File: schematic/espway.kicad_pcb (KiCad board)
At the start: 2 copper layers, 28 parts, among them J1 CONN_01X02, J2 CONN_01X02, J3 CONN_01X04_MALE, SW1 SW_Push, U1 DRV8835, U2 LM1117-3.3, U3 ESP-12E, U4 LSM6DS3

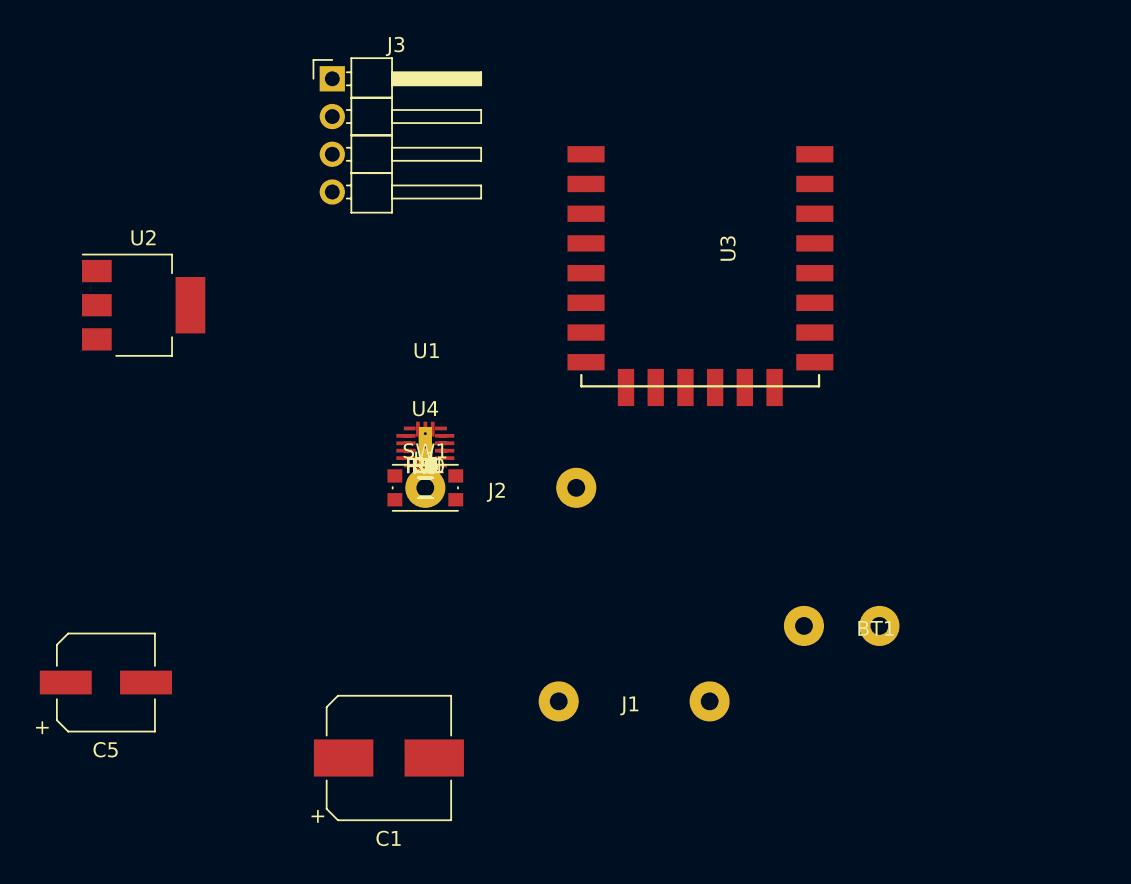
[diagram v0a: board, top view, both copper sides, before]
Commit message: Update schematic and PCB layout
Misses power led and routing
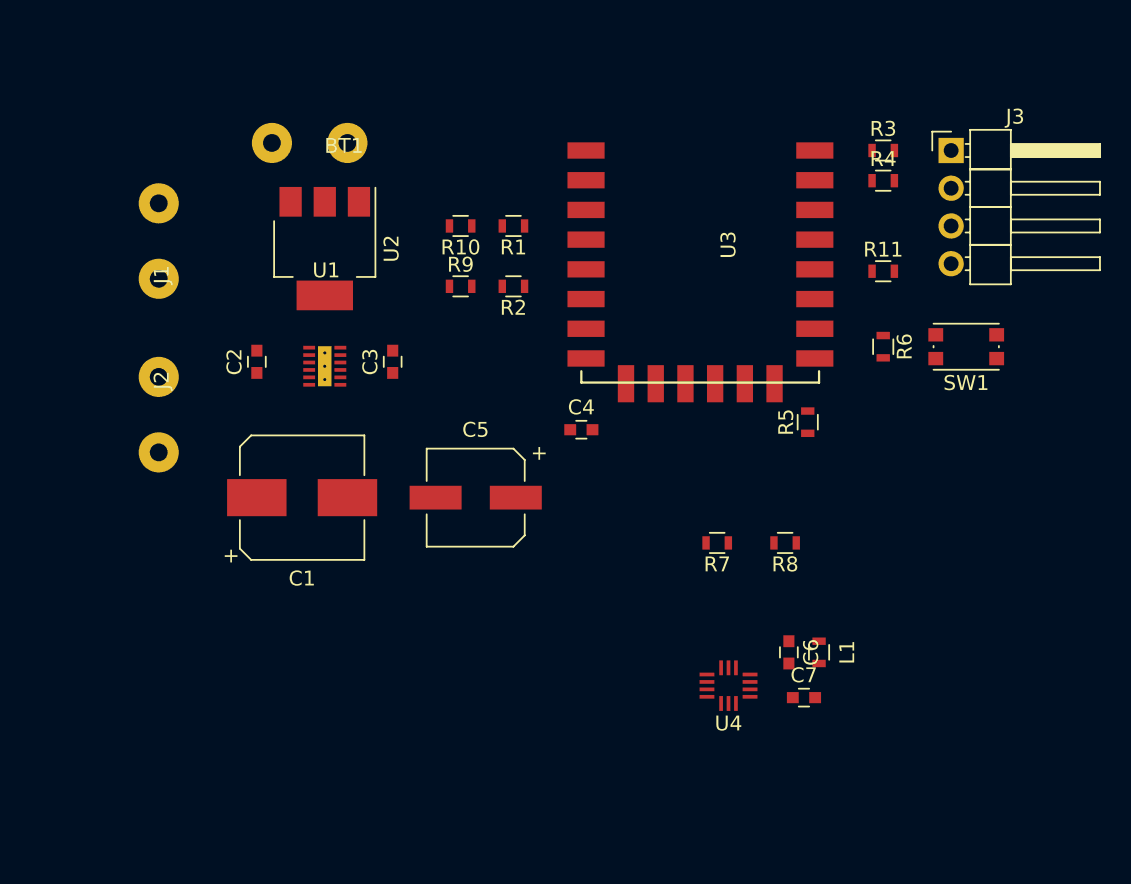
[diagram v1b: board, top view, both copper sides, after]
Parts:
- moved BT1 48.4 mm to (138.2, 81.8)
- moved J3 41.9 mm to (183.9, 82.3)
- moved R3 38.3 mm to (179.3, 82.3)
- moved SW1 37.6 mm to (184.9, 95.5), turned to 180 degrees
- moved R4 37.1 mm to (179.3, 84.3)
- moved J1 36.0 mm to (130.6, 95.5), turned to 90 degrees
- moved R11 34.1 mm to (179.3, 90.4)
- moved R6 32.3 mm to (179.3, 95.5), turned to 270 degrees
- moved C7 29.1 mm to (174.0, 119.1)
- moved L1 28.7 mm to (175.0, 116.1), turned to 270 degrees
- moved C5 27.8 mm to (151.9, 105.7), turned to 180 degrees
- moved C6 26.9 mm to (173.0, 116.1), turned to 270 degrees
- moved R5 26.1 mm to (174.2, 100.6), turned to 90 degrees
- moved R8 24.5 mm to (172.7, 108.7), turned to 180 degrees
- moved U4 23.0 mm to (168.9, 115.6), turned to 180 degrees
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
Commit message: Schematic and PCB update
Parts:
- U3: value ESP-12E -> ESP-12S
- moved C7 15.4 mm to (165.6, 106.2), turned to 270 degrees
- moved L1 9.01 mm to (169.2, 109.2), turned to 180 degrees
- moved R8 8.23 mm to (171.4, 100.6), turned to 90 degrees
- moved R7 8.14 mm to (168.7, 100.6), turned to 90 degrees
- moved U4 7.69 mm to (169.9, 108.0), turned to 0 degrees
- moved C6 6.86 mm to (173.0, 109.2), turned to 180 degrees
- moved J2 4.07 mm to (130.8, 106.7)
- moved J1 3.57 mm to (130.8, 99.1)
- moved R6 1.27 mm to (179.3, 94.2), turned to 0 degrees
- moved C4 0.51 mm to (159.0, 100.6), turned to 270 degrees

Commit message: Update schematic and PCB
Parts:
- added D1: LED, LEDs:LED_0603, F.Cu at (156.0, 98.0)
- added R12: 470, Resistors_SMD:R_0603, F.Cu at (156.2, 96.3)
- added REF**: MountingHole_2.2mm_M2, Mounting_Holes:MountingHole_2.2mm_M2, F.Cu at (177.0, 115.6)
- added REF**: MountingHole_2.2mm_M2, Mounting_Holes:MountingHole_2.2mm_M2, F.Cu at (147.3, 115.6)
- added REF**: MountingHole_2.2mm_M2, Mounting_Holes:MountingHole_2.2mm_M2, F.Cu at (147.3, 83.1)
- J1, J2: footprint Wire_Connections_Bridges:WireConnection_1.20mmDrill -> Wire_Connections_Bridges:WireConnection_1.00mmDrill
- U3: value ESP-12S -> ESP-12E
- moved BT1 42.2 mm to (165.1, 114.3)
- moved U2 29.1 mm to (156.7, 113.8), turned to 0 degrees
- moved J3 23.0 mm to (176.0, 103.9)
- moved J1 18.5 mm to (147.3, 90.8)
- moved J2 16.6 mm to (147.3, 104.8)
- moved C2 16.0 mm to (151.4, 89.2), turned to 270 degrees
- moved U1 11.7 mm to (152.7, 95.5)
- moved C3 10.6 mm to (153.9, 89.2), turned to 270 degrees
- moved C1 10.5 mm to (150.6, 104.4)
- moved C5 10.0 mm to (161.8, 104.1), turned to 0 degrees
- moved SW1 9.02 mm to (177.3, 100.3)
- moved R9 7.40 mm to (152.9, 84.3)
- moved R5 7.22 mm to (167.1, 99.3), turned to 0 degrees
- moved R1 5.38 mm to (156.2, 82.3)
- moved R2 5.38 mm to (156.2, 86.4)
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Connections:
- R3 pad 1: Net-(J3-Pad3) -> Net-(J3-Pad2)
- R4 pad 1: Net-(J3-Pad2) -> Net-(J3-Pad3)
- U1 pad 13: (no net) -> GND
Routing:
- net GND: track 0.00 -> 103.5 mm, vias 0 -> 10
- net +3V3: track 0.00 -> 91.2 mm, vias 0 -> 4
- net +BATT: track 0.00 -> 74.0 mm, vias 0 -> 4
- net Net-(J3-Pad3): track 0.00 -> 26.7 mm, vias 0 -> 1
- net Net-(J3-Pad2): track 0.00 -> 25.4 mm, vias 0 -> 1
- net GPIO15: track 0.00 -> 24.5 mm, vias 0 -> 2
- net SCL: track 0.00 -> 21.3 mm
- net SDA: track 0.00 -> 19.9 mm, vias 0 -> 2
- net INT: track 0.00 -> 17.8 mm, vias 0 -> 2
- net Net-(R11-Pad2): track 0.00 -> 13.7 mm
- net Net-(R5-Pad2): track 0.00 -> 12.4 mm, vias 0 -> 2
- net ADC: track 0.00 -> 8.15 mm
- net Net-(U1-Pad10): track 0.00 -> 7.23 mm
- net Net-(J1-Pad2): track 0.00 -> 6.67 mm
- net Net-(U1-Pad8): track 0.00 -> 6.64 mm
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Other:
- board outline added: 36.2 x 38.7 mm
- net class power added: clearance 0.2, trace_width 0.5, via_dia 0.6, via_drill 0.4

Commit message: Update PCB
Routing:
- net GND: track 103.5 -> 24.7 mm, vias 10 -> 9
- net +BATT: track 74.0 -> 11.8 mm
- net Net-(J1-Pad2): track 6.67 -> 0.75 mm
- net Net-(J2-Pad1): track 6.48 -> 1.00 mm
- net Net-(J2-Pad2): track 4.95 -> 0.89 mm
- net Net-(J1-Pad1): track 4.99 -> 1.56 mm
- net +3V3: track 91.2 -> 88.3 mm
- added copper zone on B.Cu, net +BATT
- added copper zone on B.Cu, net GND
- added copper zone on F.Cu, net GND
- added copper zone on F.Cu, net Net-(J1-Pad1)
- added copper zone on F.Cu, net Net-(J1-Pad2)
- added copper zone on F.Cu, net Net-(J2-Pad1)
- added copper zone on F.Cu, net Net-(J2-Pad2)
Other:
- net class power: trace_width 0.5 -> 0.25

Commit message: Update PCB
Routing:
- net GND: track 24.7 -> 29.1 mm, vias 9 -> 14
- net +3V3: track 88.3 -> 92.1 mm, vias 4 -> 3
- net +BATT: track 11.8 -> 10.5 mm, vias 4 -> 6
- net Net-(J2-Pad2): track 0.89 -> 1.68 mm
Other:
- net class Default: clearance 0.2 -> 0.16
- net class power removed
- rule trace_clearance: 0.2 -> 0.16

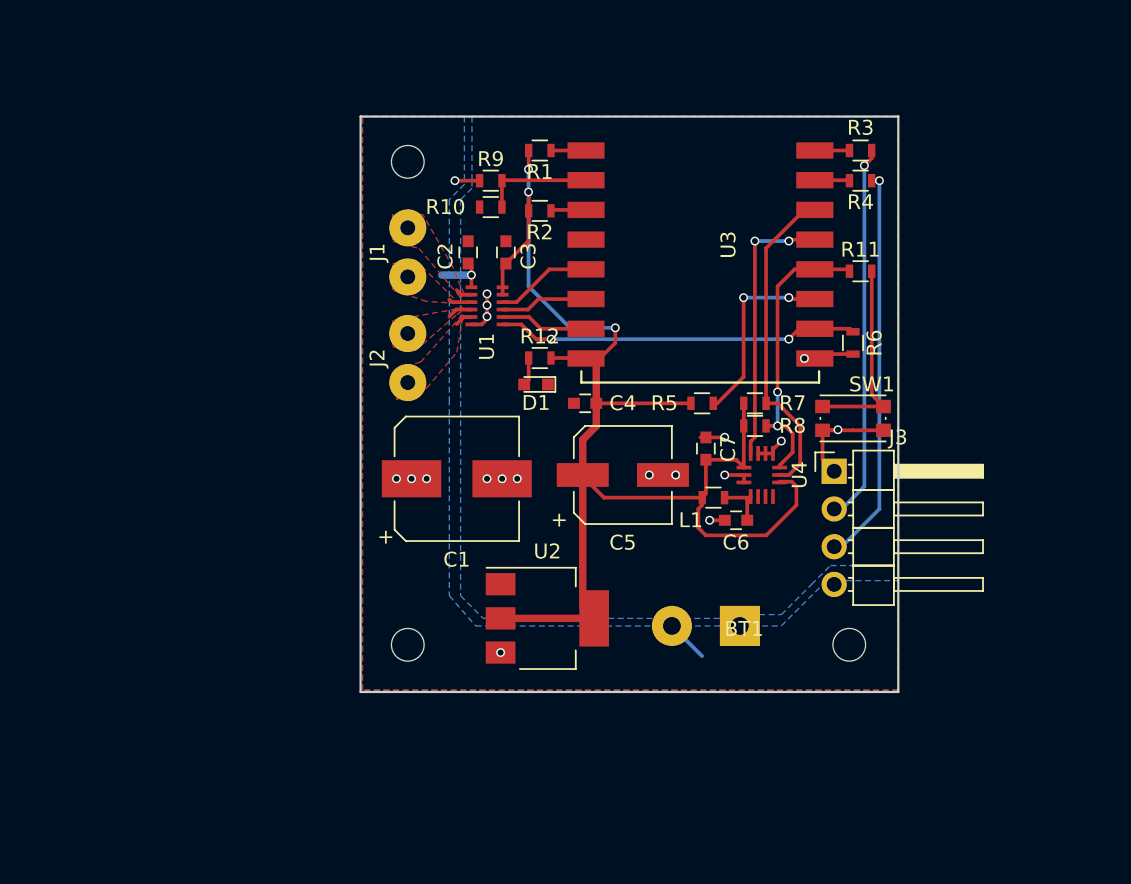
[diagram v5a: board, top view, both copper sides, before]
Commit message: Plenty of updates to PCB
* Fix bug where one motor would spin in bootloader
* Add helpful labels
* Add another via for V+ near motor driver
* Larger screw holes
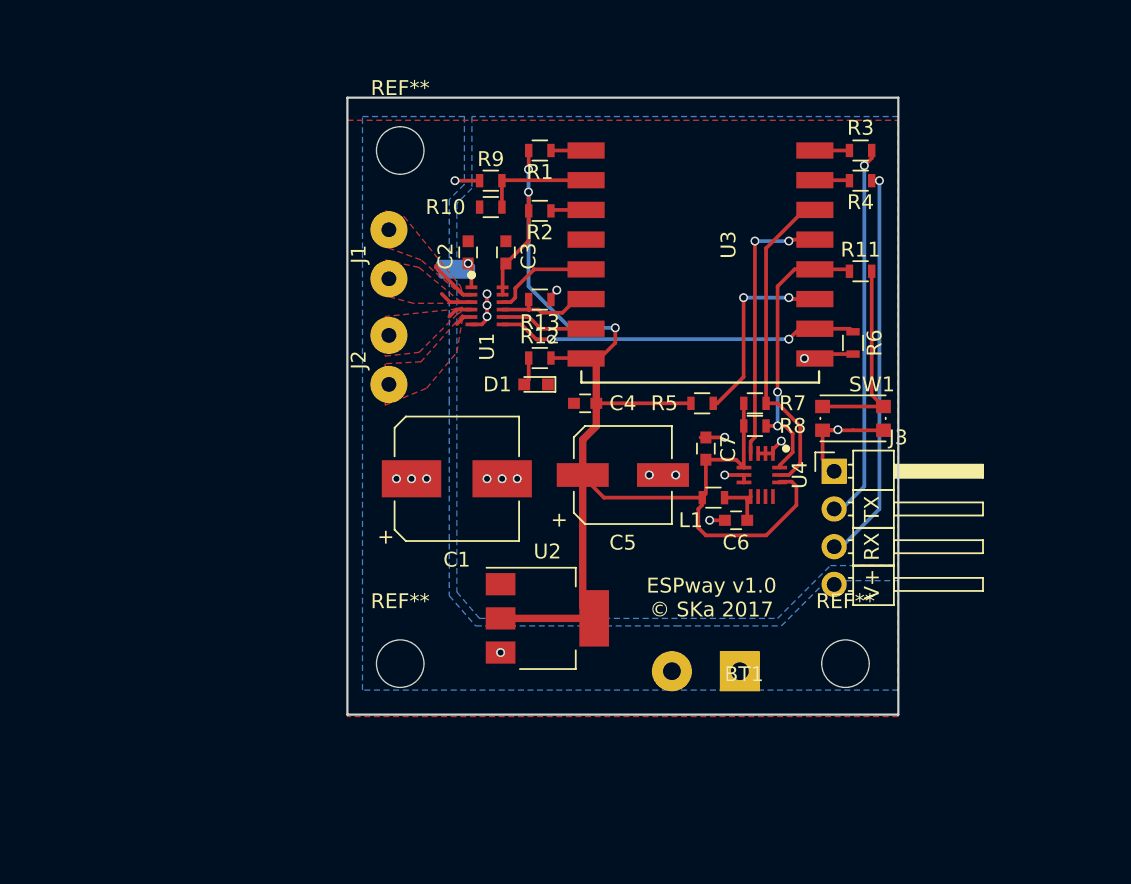
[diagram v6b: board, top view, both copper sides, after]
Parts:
- added R13: 10k, Resistors_SMD:R_0603, F.Cu at (156.2, 92.3)
- REF** (x3): footprint Mounting_Holes:MountingHole_2.2mm_M2 -> Mounting_Holes:MountingHole_3.2mm_M3
- moved BT1 3.05 mm to (165.1, 117.3)
- moved REF** 1.37 mm to (146.8, 116.8)
- moved REF** 1.30 mm to (176.8, 116.8)
- moved J1 1.28 mm to (146.1, 90.9)
- moved J2 1.28 mm to (146.1, 104.9)
- moved REF** 0.92 mm to (146.8, 82.3)
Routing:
- net Net-(R13-Pad1): track 6.61 -> 9.15 mm
- net +BATT: track 10.5 -> 12.7 mm, vias 6 -> 7
- net Net-(J1-Pad2): track 1.11 -> 3.27 mm
- net GND: track 29.1 -> 27.7 mm, vias 14 -> 15
- net Net-(J1-Pad1): track 1.56 -> 2.23 mm
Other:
- board size 36.2 x 38.7 mm -> 37.1 x 41.5 mm
- board text added: "ESPway v1.0 © SKa 2017"
- board text added: "GND"
- board text added: "RX"
- board text added: "TX"
- board text added: "V+"

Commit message: Aesthetic changes to PCB
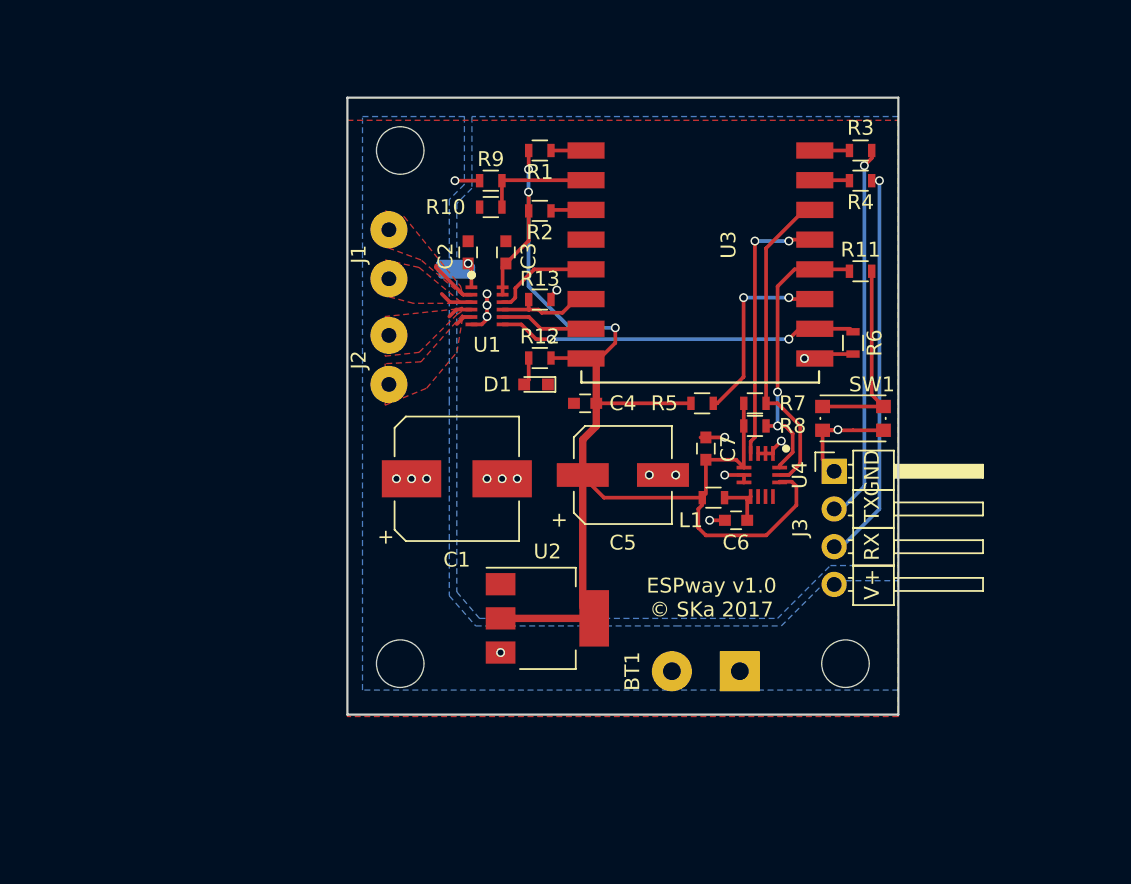
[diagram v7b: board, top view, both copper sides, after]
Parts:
- renumbered REF** to ?
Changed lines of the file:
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@@
     (links 75)
     (no_connects 0)
-    (area 143.180999 78.664999 180.415001 120.344001)
+    (area 137.294857 73.360999 187.568429 122.193)
     (thickness 1.6)
     (drawings 11)
@@
     (visible_elements 7FFFFFFF)
     (pcbplotparams
-      (layerselection 0x011fc_80000001)
+      (layerselection 0x010f0_80000001)
       (usegerberextensions true)
       (excludeedgelayer true)
@@
     (tags "mounting hole 3.2mm no annular m3")
     (attr virtual)
-    (fp_text reference REF** (at 0 -4.2) (layer F.SilkS)
+    (fp_text reference REF** (at 0 -4.2) (layer F.SilkS) hide
       (effects (font (size 1 1) (thickness 0.15)))
     )
@@
     (tags "mounting hole 3.2mm no annular m3")
     (attr virtual)
-    (fp_text reference REF** (at 0 -4.2) (layer F.SilkS)
+    (fp_text reference "" (at 0 -4.2) (layer F.SilkS) hide
       (effects (font (size 1 1) (thickness 0.15)))
     )
@@
     (tags "mounting hole 3.2mm no annular m3")
     (attr virtual)
-    (fp_text reference REF** (at 0 -4.2) (layer F.SilkS)
+    (fp_text reference REF** (at 0 -4.2) (layer F.SilkS) hide
       (effects (font (size 1 1) (thickness 0.15)))
     )
@@
     (at 165.1 117.348)
     (descr "WireConnection with 1.2mm drill")
-    (fp_text reference BT1 (at 4.8514 0.2032) (layer F.SilkS)
+    (fp_text reference BT1 (at -2.667 0 90) (layer F.SilkS)
       (effects (font (size 1 1) (thickness 0.15)))
     )
@@
     (descr "Through hole angled pin header, 1x04, 2.54mm pitch, 6mm pin length, single row")
     (tags "Through hole angled pin header THT 1x04 2.54mm single row")
-    (fp_text reference J3 (at 4.315 -2.27) (layer F.SilkS)
+    (fp_text reference J3 (at -2.286 3.81 90) (layer F.SilkS)
       (effects (font (size 1 1) (thickness 0.15)))
     )
@@
   (module espway-modules:WSON-12 (layer F.Cu)
     (at 152.654 95.504)
-    (fp_text reference U1 (at 0 0 90) (layer F.SilkS)
+    (fp_text reference U1 (at 0 -0.127 180) (layer F.SilkS)
       (effects (font (size 1 1) (thickness 0.15)))
     )
@@
     (tags "resistor 0603")
     (attr smd)
-    (fp_text reference R13 (at 0 1.524) (layer F.SilkS)
+    (fp_text reference R13 (at 0 -1.397) (layer F.SilkS)
       (effects (font (size 1 1) (thickness 0.15)))
     )
@@
     (effects (font (size 1 1) (thickness 0.25)))
   )
-  (gr_text GND (at 178.562 104.013 90) (layer B.SilkS)
+  (gr_text GND (at 178.562 104.013 90) (layer F.SilkS)
     (effects (font (size 1 1) (thickness 0.25)))
   )

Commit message: Decrease I2C pullups to 2k2 (UNTESTED but should work better)
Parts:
- R7, R8: value 10k -> 2k2
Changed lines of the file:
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@@
     (links 75)
     (no_connects 0)
-    (area 137.294857 73.360999 187.568429 122.193)
+    (area 143.180999 78.664999 180.415001 120.344001)
     (thickness 1.6)
     (drawings 11)
@@
   )
   (setup
-    (last_trace_width 0.5)
+    (last_trace_width 0.25)
     (user_trace_width 0.5)
     (trace_clearance 0.16)
@@
     (pad_to_mask_clearance 0.2)
     (aux_axis_origin 0 0)
+    (grid_origin 143.256 120.142)
     (visible_elements 7FFFFFFF)
     (pcbplotparams
@@
       (drillshape 0)
       (scaleselection 1)
-      (outputdirectory ""))
+      (outputdirectory plot/))
   )
   (net 0 "")
@@
       (effects (font (size 1 1) (thickness 0.15)))
     )
-    (fp_text value 10k (at 0 1.5) (layer F.Fab)
+    (fp_text value 2k2 (at 0 1.5) (layer F.Fab)
       (effects (font (size 1 1) (thickness 0.15)))
     )
@@
       (effects (font (size 1 1) (thickness 0.15)))
     )
-    (fp_text value 10k (at 0 1.5) (layer F.Fab)
-      (effects (font (size 1 1) (thickness 0.15)))
-    )
+    (fp_text value 2k2 (at 0 1.5) (layer F.Fab)
+      (effects (font (size 1 1) (thickness 0.15)))
+    )
